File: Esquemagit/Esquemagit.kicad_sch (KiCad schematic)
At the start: 27 parts, among them J2 UJ20-C-H-G-MSMT-9B-P16-TR, U1 LMV321, U2 AMS1117-3.3, U5 ESP32-WROOM-32

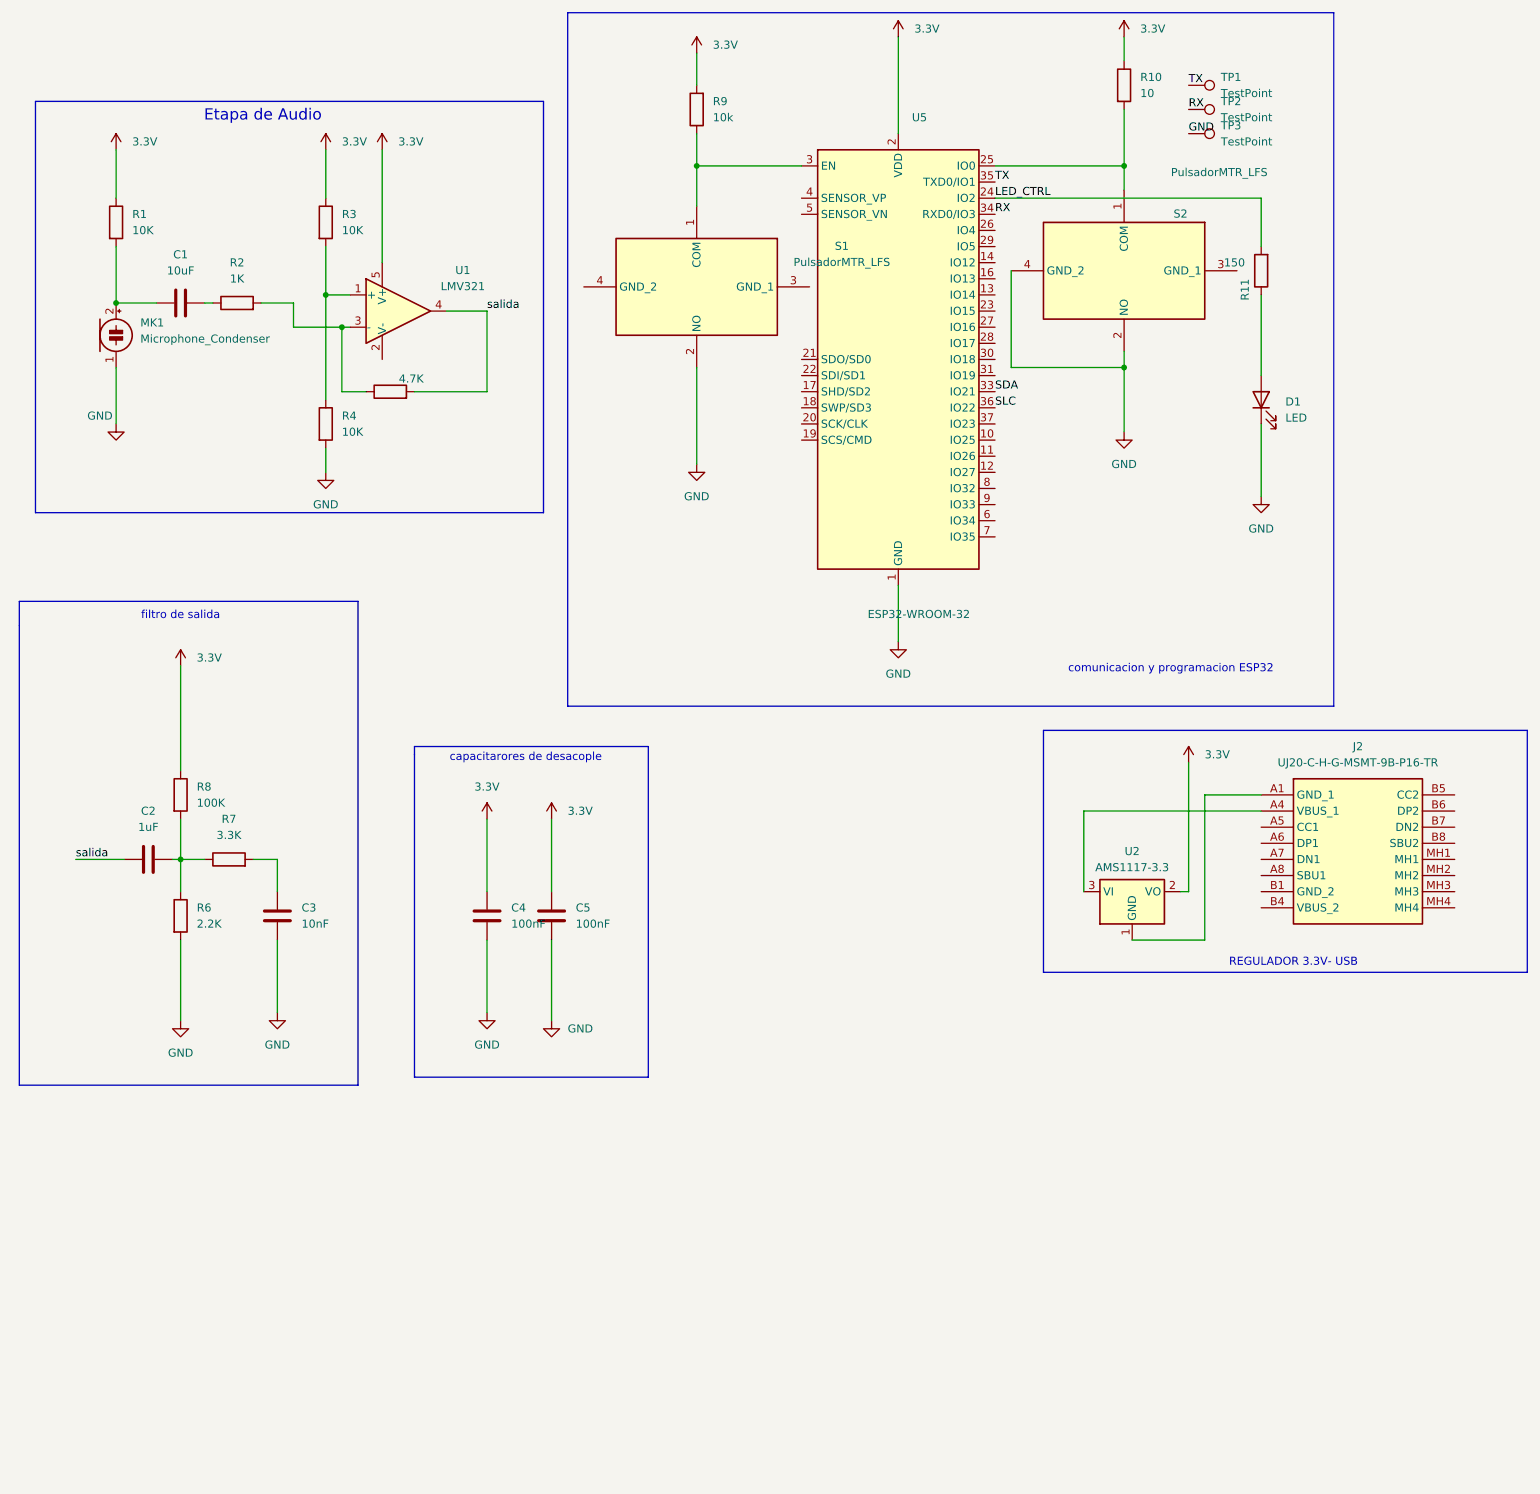
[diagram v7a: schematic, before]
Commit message: fix: se corrigieron elementos en el esquematico
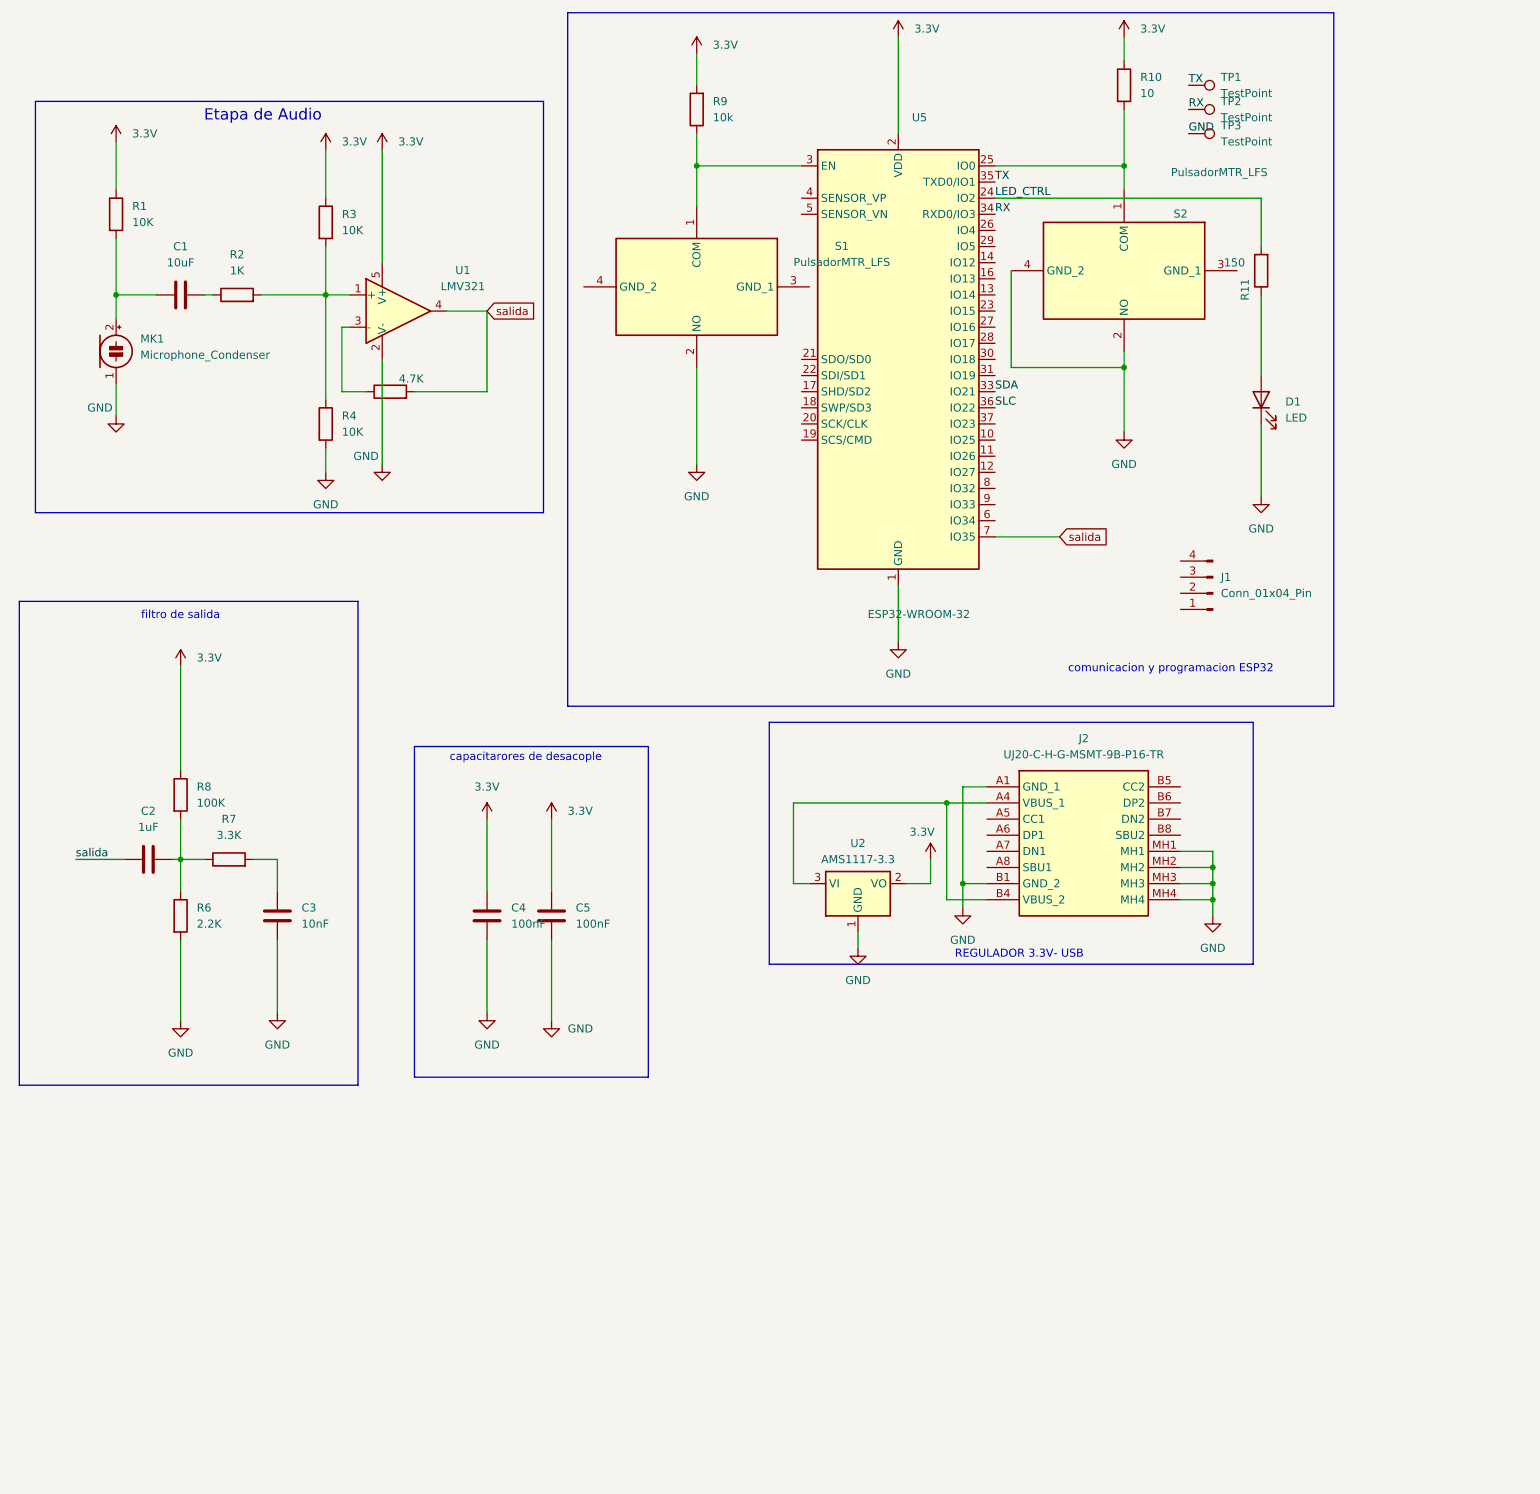
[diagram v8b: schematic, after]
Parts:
- added J1: Conn_01x04_Pin, Connector:FanPinHeader_1x04_P2.54mm_Vertical, symbol Connector:Conn_01x04_Pin
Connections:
- net GND: now also J2.A1 (GND_1), J2.B1 (GND_2), J2.MH1, J2.MH2, J2.MH3, J2.MH4, U1.2 (V-), U2.1 (GND)
- net salida: now also U5.7 (IO35)
- net at J2.A4 (VBUS_1), U2.3 (VI): now also J2.B4 (VBUS_2)
- net at R3.2, R4.1, U1.1 (+): now also R2.2
- net at R5.1, U1.3 (-): no longer R2.2
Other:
- moved on the sheet: C1, J2, MK1, R1, R2, U2
